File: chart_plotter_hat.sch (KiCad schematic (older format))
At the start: 38 parts, among them J1 Conn_02x03_Odd_Even, J2 Conn_01x04, J3 40HAT, J4 Conn_01x04, J5 Conn_01x04, J6 Conn_01x02, J7 Conn_01x04, J8 Conn_02x03_Odd_Even, Q1 DMG2305UX, Q2 DMMT5401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

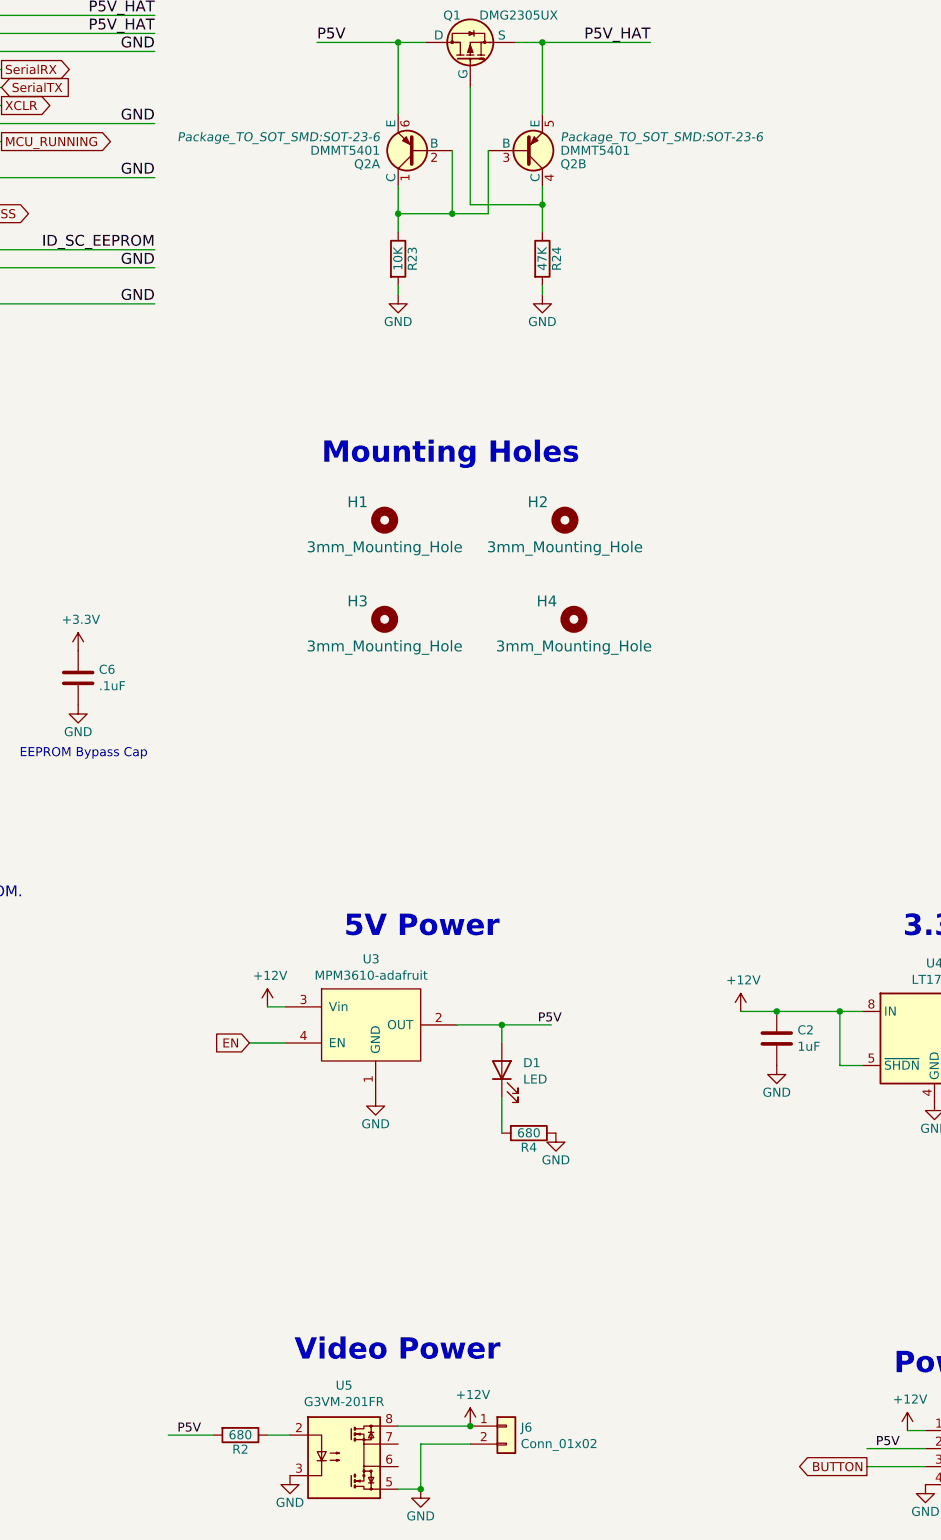
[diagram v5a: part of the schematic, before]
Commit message: Fixed relay net
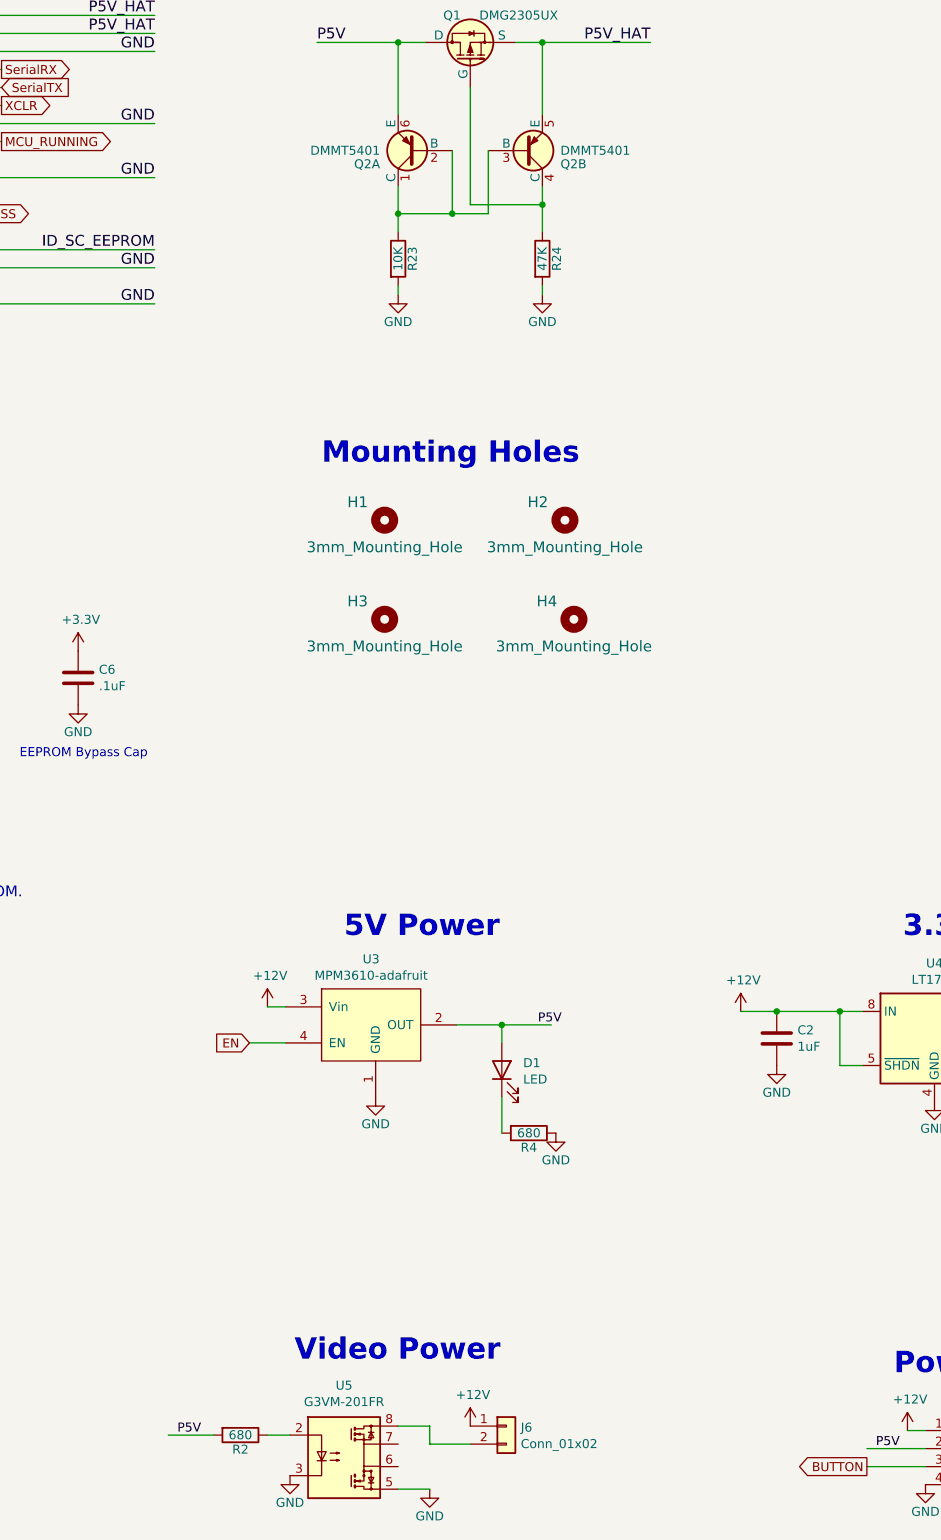
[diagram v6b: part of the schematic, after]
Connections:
- net +12V: no longer U5.8
- net GND: no longer J6.2 (Pin_2)
- new net: J6.2 (Pin_2), U5.8
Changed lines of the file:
@@
 F 0 "Q2" H 6050 3075 50  0000 L CNN
 F 1 "DMMT5401" H 6050 3000 50  0000 L CNN
-F 2 "Package_TO_SOT_SMD:SOT-23-6" H 6050 2925 50  0000 L CIN
+F 2 "Package_TO_SOT_SMD:SOT-23-6" H 6050 2925 50  0001 L CIN
 F 3 "" H 5850 3000 50  0000 L CNN
 	1    5850 3000
@@
 F 0 "Q2" H 6650 3075 50  0000 L CNN
 F 1 "DMMT5401" H 6650 3000 50  0000 L CNN
-F 2 "Package_TO_SOT_SMD:SOT-23-6" H 6650 2925 50  0000 L CIN
+F 2 "Package_TO_SOT_SMD:SOT-23-6" H 6650 2925 50  0001 L CIN
 F 3 "" H 6450 3000 50  0000 L CNN
 	2    6450 3000
@@
 Wire Wire Line
 	5025 10125 5150 10125
-Wire Wire Line
-	6150 10075 5750 10075
-Wire Wire Line
-	6150 10175 5875 10175
-Wire Wire Line
-	5875 10175 5875 10425
-Wire Wire Line
-	5875 10425 5750 10425
-Connection ~ 5875 10425
-Connection ~ 6150 10075
-$Comp
-L power:GND #PWR0111
-U 1 1 5FF51245
-P 5875 10425
-F 0 "#PWR0111" H 5875 10175 50  0001 C CNN
-F 1 "GND" H 5875 10275 50  0000 C CNN
-F 2 "" H 5875 10425 50  0000 C CNN
-F 3 "" H 5875 10425 50  0000 C CNN
-	1    5875 10425
-	1    0    0    -1
-$EndComp
 $Comp
 L Connector_Generic:Conn_01x04 J4
@@
 Connection ~ 13050 8025
 $Comp
-L power:GND #PWR?
+L power:GND #PWR0111
 U 1 1 5FFA1E86
 P 11050 8300
-F 0 "#PWR?" H 11050 8050 50  0001 C CNN
+F 0 "#PWR0111" H 11050 8050 50  0001 C CNN
 F 1 "GND" H 11050 8150 50  0000 C CNN
 F 2 "" H 11050 8300 50  0000 C CNN
@@
 	1    0    0    -1
 $EndComp
+Wire Wire Line
+	6150 10175 5925 10175
+Wire Wire Line
+	5925 10175 5925 10075
+Wire Wire Line
+	5925 10075 5750 10075
+Wire Wire Line
+	5750 10425 5925 10425
+$Comp
+L power:GND #PWR0118
+U 1 1 5FF48764
+P 5925 10425
+F 0 "#PWR0118" H 5925 10175 50  0001 C CNN
+F 1 "GND" H 5925 10275 50  0000 C CNN
+F 2 "" H 5925 10425 50  0000 C CNN
+F 3 "" H 5925 10425 50  0000 C CNN
+	1    5925 10425
+	1    0    0    -1
+$EndComp

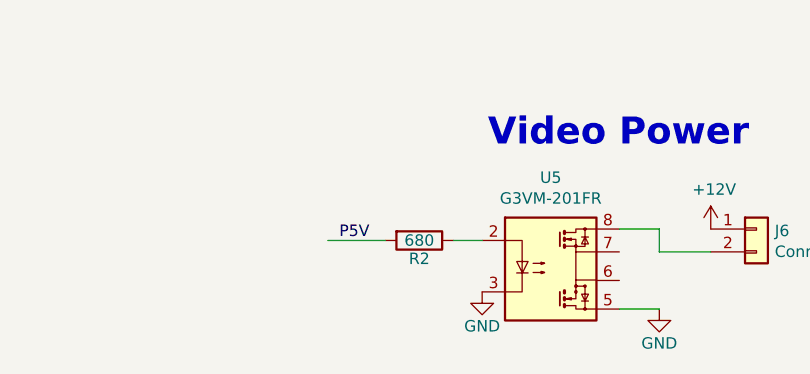
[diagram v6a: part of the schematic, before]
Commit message: Moved R2 resistor to ground side of relay circuit
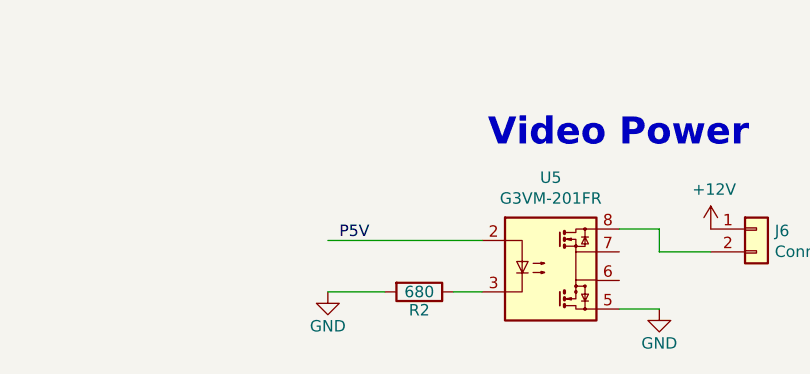
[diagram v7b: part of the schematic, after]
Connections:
- net GND: now also R2.2; no longer U5.3
- net P5V: now also U5.2; no longer R2.2
- net at R2.1: now also U5.3; no longer U5.2
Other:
- moved on the sheet: R2
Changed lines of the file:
@@
 L power:GND #PWR0113
 U 1 1 5FF37278
-P 5150 10350
-F 0 "#PWR0113" H 5150 10100 50  0001 C CNN
-F 1 "GND" H 5150 10200 50  0000 C CNN
-F 2 "" H 5150 10350 50  0000 C CNN
-F 3 "" H 5150 10350 50  0000 C CNN
-	1    5150 10350
+P 4475 10350
+F 0 "#PWR0113" H 4475 10100 50  0001 C CNN
+F 1 "GND" H 4475 10200 50  0000 C CNN
+F 2 "" H 4475 10350 50  0000 C CNN
+F 3 "" H 4475 10350 50  0000 C CNN
+	1    4475 10350
 	1    0    0    -1
 $EndComp
@@
 L Device:R R2
 U 1 1 5FF8607A
-P 4875 10125
-F 0 "R2" V 4955 10125 50  0000 C CNN
-F 1 "680" V 4875 10125 50  0000 C CNN
-F 2 "Resistors_SMD:R_0603" V 4805 10125 50  0001 C CNN
-F 3 "" H 4875 10125 50  0001 C CNN
-	1    4875 10125
+P 4875 10350
+F 0 "R2" V 4955 10350 50  0000 C CNN
+F 1 "680" V 4875 10350 50  0000 C CNN
+F 2 "Resistors_SMD:R_0603" V 4805 10350 50  0001 C CNN
+F 3 "" H 4875 10350 50  0001 C CNN
+	1    4875 10350
 	0    1    1    0
 $EndComp
@@
 	1    0    0    -1
 $EndComp
-Wire Wire Line
-	4725 10125 4475 10125
 Text Label 4525 10125 0    50   ~ 0
 P5V
@@
 	1    0    0    -1
 $EndComp
-Wire Wire Line
-	5025 10125 5150 10125
 $Comp
 L Connector_Generic:Conn_01x04 J4
@@
 	1    0    0    -1
 $EndComp
+Wire Wire Line
+	5025 10350 5150 10350
+Wire Wire Line
+	4725 10350 4475 10350
+Wire Wire Line
+	4475 10125 5150 10125
 $EndSCHEMATC

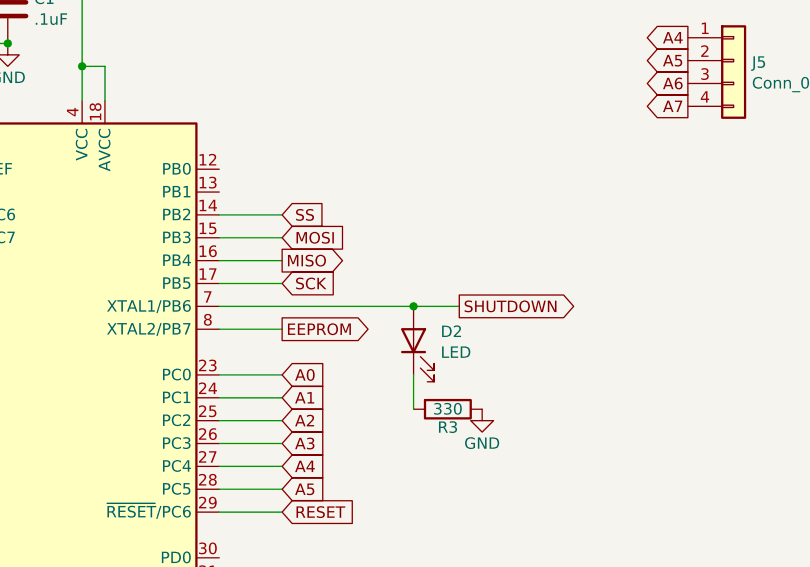
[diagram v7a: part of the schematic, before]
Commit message: Moved second led to MISO instead of shutdown
Cleaned up some via's
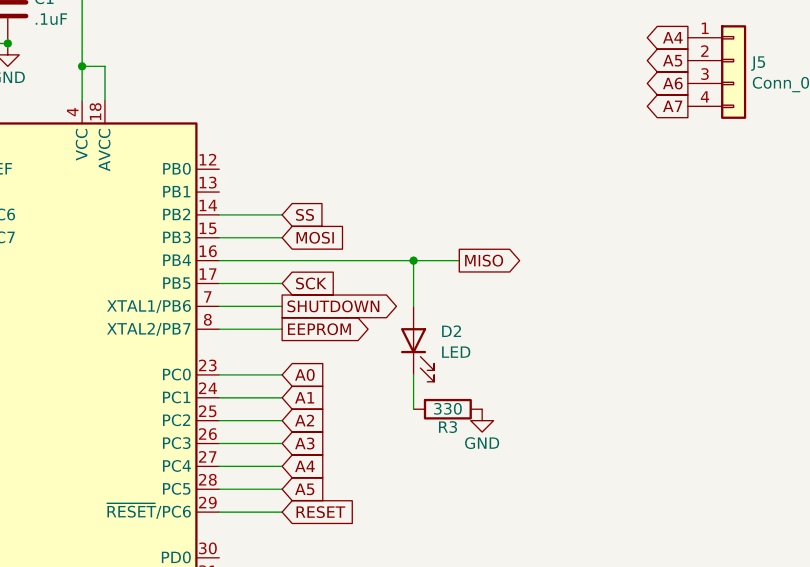
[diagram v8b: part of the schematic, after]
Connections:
- net MISO: now also D2.2 (A)
- net SHUTDOWN: no longer D2.2 (A)
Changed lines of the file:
@@
 Text GLabel 12550 6100 2    50   Input ~ 0
 SCK
-Text GLabel 12550 6000 2    50   Output ~ 0
+Text GLabel 13325 6000 2    50   Output ~ 0
 MISO
 Text GLabel 12550 5900 2    50   Input ~ 0
@@
 Wire Wire Line
 	12275 5900 12550 5900
-Wire Wire Line
-	12275 6000 12550 6000
 Wire Wire Line
 	12275 6100 12550 6100
@@
 	1    0    0    -1
 $EndComp
-Text GLabel 13325 6200 2    50   Output ~ 0
+Text GLabel 12550 6200 2    50   Output ~ 0
 SHUTDOWN
 Text GLabel 13225 8025 2    50   Input ~ 0
@@
 Wire Wire Line
 	12275 7500 13250 7500
-Wire Wire Line
-	12275 6200 13125 6200
 $Comp
 L power:GND #PWR015
@@
 Wire Wire Line
 	4925 7950 5125 7950
-Connection ~ 13125 6200
-Wire Wire Line
-	13125 6200 13325 6200
 Wire Wire Line
 	13125 6500 13125 6650
@@
 Wire Wire Line
 	4475 10125 5150 10125
+Wire Wire Line
+	12275 6200 12550 6200
+Wire Wire Line
+	12275 6000 13125 6000
+Wire Wire Line
+	13125 6200 13125 6000
+Connection ~ 13125 6000
+Wire Wire Line
+	13125 6000 13325 6000
 $EndSCHEMATC
